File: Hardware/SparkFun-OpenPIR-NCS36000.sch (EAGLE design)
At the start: 33 parts, among them U1 NCS36000, U2 PIR

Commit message: Adding test points to trimpot wipers
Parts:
- added TP1, TP2: TEST-POINT3X5, SparkFun-Connectors:TEST-POINT3X5
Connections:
- net N$7: now also TP1.1
- net VCC: now also TP2.1
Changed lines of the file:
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@@
 <grid distance="0.1" unitdist="inch" unit="inch" style="lines" multiple="1" display="no" altdistance="0.01" altunitdist="inch" altunit="inch"/>
 <layers>
-<layer number="1" name="Top" color="4" fill="1" visible="no" active="no"/>
-<layer number="2" name="Route2" color="1" fill="3" visible="no" active="no"/>
-<layer number="3" name="Route3" color="4" fill="3" visible="no" active="no"/>
-<layer number="4" name="Route4" color="1" fill="4" visible="no" active="no"/>
-<layer number="5" name="Route5" color="4" fill="4" visible="no" active="no"/>
-<layer number="6" name="Route6" color="1" fill="8" visible="no" active="no"/>
-<layer number="7" name="Route7" color="4" fill="8" visible="no" active="no"/>
-<layer number="8" name="Route8" color="1" fill="2" visible="no" active="no"/>
-<layer number="9" name="Route9" color="4" fill="2" visible="no" active="no"/>
-<layer number="10" name="Route10" color="1" fill="7" visible="no" active="no"/>
-<layer number="11" name="Route11" color="4" fill="7" visible="no" active="no"/>
-<layer number="12" name="Route12" color="1" fill="5" visible="no" active="no"/>
-<layer number="13" name="Route13" color="4" fill="5" visible="no" active="no"/>
-<layer number="14" name="Route14" color="1" fill="6" visible="no" active="no"/>
-<layer number="15" name="Route15" color="4" fill="6" visible="no" active="no"/>
-<layer number="16" name="Bottom" color="1" fill="1" visible="no" active="no"/>
-<layer number="17" name="Pads" color="2" fill="1" visible="no" active="no"/>
-<layer number="18" name="Vias" color="2" fill="1" visible="no" active="no"/>
-<layer number="19" name="Unrouted" color="6" fill="1" visible="no" active="no"/>
-<layer number="20" name="Dimension" color="15" fill="1" visible="no" active="no"/>
-<layer number="21" name="tPlace" color="16" fill="1" visible="no" active="no"/>
-<layer number="22" name="bPlace" color="14" fill="1" visible="no" active="no"/>
-<layer number="23" name="tOrigins" color="15" fill="1" visible="no" active="no"/>
-<layer number="24" name="bOrigins" color="15" fill="1" visible="no" active="no"/>
-<layer number="25" name="tNames" color="7" fill="1" visible="no" active="no"/>
-<layer number="26" name="bNames" color="7" fill="1" visible="no" active="no"/>
-<layer number="27" name="tValues" color="7" fill="1" visible="no" active="no"/>
-<layer number="28" name="bValues" color="7" fill="1" visible="no" active="no"/>
+<layer number="1" name="Top" color="4" fill="1" visible="yes" active="no"/>
+<layer number="2" name="Route2" color="1" fill="3" visible="yes" active="no"/>
+<layer number="3" name="Route3" color="4" fill="3" visible="yes" active="no"/>
+<layer number="4" name="Route4" color="1" fill="4" visible="yes" active="no"/>
+<layer number="5" name="Route5" color="4" fill="4" visible="yes" active="no"/>
+<layer number="6" name="Route6" color="1" fill="8" visible="yes" active="no"/>
+<layer number="7" name="Route7" color="4" fill="8" visible="yes" active="no"/>
+<layer number="8" name="Route8" color="1" fill="2" visible="yes" active="no"/>
+<layer number="9" name="Route9" color="4" fill="2" visible="yes" active="no"/>
+<layer number="10" name="Route10" color="1" fill="7" visible="yes" active="no"/>
+<layer number="11" name="Route11" color="4" fill="7" visible="yes" active="no"/>
+<layer number="12" name="Route12" color="1" fill="5" visible="yes" active="no"/>
+<layer number="13" name="Route13" color="4" fill="5" visible="yes" active="no"/>
+<layer number="14" name="Route14" color="1" fill="6" visible="yes" active="no"/>
+<layer number="15" name="Route15" color="4" fill="6" visible="yes" active="no"/>
+<layer number="16" name="Bottom" color="1" fill="1" visible="yes" active="no"/>
+<layer number="17" name="Pads" color="2" fill="1" visible="yes" active="no"/>
+<layer number="18" name="Vias" color="2" fill="1" visible="yes" active="no"/>
+<layer number="19" name="Unrouted" color="6" fill="1" visible="yes" active="no"/>
+<layer number="20" name="Dimension" color="15" fill="1" visible="yes" active="no"/>
+<layer number="21" name="tPlace" color="16" fill="1" visible="yes" active="no"/>
+<layer number="22" name="bPlace" color="14" fill="1" visible="yes" active="no"/>
+<layer number="23" name="tOrigins" color="15" fill="1" visible="yes" active="no"/>
+<layer number="24" name="bOrigins" color="15" fill="1" visible="yes" active="no"/>
+<layer number="25" name="tNames" color="7" fill="1" visible="yes" active="no"/>
+<layer number="26" name="bNames" color="7" fill="1" visible="yes" active="no"/>
+<layer number="27" name="tValues" color="7" fill="1" visible="yes" active="no"/>
+<layer number="28" name="bValues" color="7" fill="1" visible="yes" active="no"/>
 <layer number="29" name="tStop" color="7" fill="3" visible="no" active="no"/>
 <layer number="30" name="bStop" color="7" fill="6" visible="no" active="no"/>
@@
 <layer number="35" name="tGlue" color="7" fill="4" visible="no" active="no"/>
 <layer number="36" name="bGlue" color="7" fill="5" visible="no" active="no"/>
-<layer number="37" name="tTest" color="7" fill="1" visible="no" active="no"/>
-<layer number="38" name="bTest" color="7" fill="1" visible="no" active="no"/>
+<layer number="37" name="tTest" color="7" fill="1" visible="yes" active="no"/>
+<layer number="38" name="bTest" color="7" fill="1" visible="yes" active="no"/>
 <layer number="39" name="tKeepout" color="4" fill="11" visible="no" active="no"/>
 <layer number="40" name="bKeepout" color="1" fill="11" visible="no" active="no"/>
@@
 <layer number="44" name="Drills" color="7" fill="1" visible="no" active="no"/>
 <layer number="45" name="Holes" color="7" fill="1" visible="no" active="no"/>
-<layer number="46" name="Milling" color="3" fill="1" visible="no" active="no"/>
-<layer number="47" name="Measures" color="7" fill="1" visible="no" active="no"/>
-<layer number="48" name="Document" color="7" fill="1" visible="no" active="no"/>
-<layer number="49" name="Reference" color="7" fill="1" visible="no" active="no"/>
-<layer number="50" name="dxf" color="7" fill="1" visible="no" active="no"/>
-<layer number="51" name="tDocu" color="6" fill="1" visible="no" active="no"/>
-<layer number="52" name="bDocu" color="7" fill="1" visible="no" active="no"/>
-<layer number="53" name="tGND_GNDA" color="7" fill="9" visible="no" active="no"/>
-<layer number="54" name="bGND_GNDA" color="1" fill="9" visible="no" active="no"/>
-<layer number="56" name="wert" color="7" fill="1" visible="no" active="no"/>
-<layer number="57" name="tCAD" color="7" fill="1" visible="no" active="no"/>
-<layer number="59" name="tCarbon" color="7" fill="1" visible="no" active="no"/>
-<layer number="60" name="bCarbon" color="7" fill="1" visible="no" active="no"/>
+<layer number="46" name="Milling" color="3" fill="1" visible="yes" active="no"/>
+<layer number="47" name="Measures" color="7" fill="1" visible="yes" active="no"/>
+<layer number="48" name="Document" color="7" fill="1" visible="yes" active="no"/>
+<layer number="49" name="Reference" color="7" fill="1" visible="yes" active="no"/>
+<layer number="50" name="dxf" color="7" fill="1" visible="yes" active="no"/>
+<layer number="51" name="tDocu" color="6" fill="1" visible="yes" active="no"/>
+<layer number="52" name="bDocu" color="7" fill="1" visible="yes" active="no"/>
+<layer number="53" name="tGND_GNDA" color="7" fill="9" visible="yes" active="no"/>
+<layer number="54" name="bGND_GNDA" color="1" fill="9" visible="yes" active="no"/>
+<layer number="56" name="wert" color="7" fill="1" visible="yes" active="no"/>
+<layer number="57" name="tCAD" color="7" fill="1" visible="yes" active="no"/>
+<layer number="59" name="tCarbon" color="7" fill="1" visible="yes" active="no"/>
+<layer number="60" name="bCarbon" color="7" fill="1" visible="yes" active="no"/>
 <layer number="90" name="Modules" color="5" fill="1" visible="yes" active="yes"/>
 <layer number="91" name="Nets" color="2" fill="1" visible="yes" active="yes"/>
@@
 <part name="FD1" library="SparkFun-Aesthetics" deviceset="FIDUCIAL" device="UFIDUCIAL"/>
 <part name="FD2" library="SparkFun-Aesthetics" deviceset="FIDUCIAL" device="UFIDUCIAL"/>
+<part name="TP1" library="SparkFun-Connectors" deviceset="TEST-POINT" device="3X5" value=""/>
+<part name="TP2" library="SparkFun-Connectors" deviceset="TEST-POINT" device="3X5" value=""/>
 </parts>
 <sheets>
@@
 <instance part="FD1" gate="G$1" x="241.3" y="25.4"/>
 <instance part="FD2" gate="G$1" x="238.76" y="27.94"/>
+<instance part="TP1" gate="G$1" x="71.12" y="127" smashed="yes">
+<attribute name="NAME" x="71.12" y="128.016" size="1.778" layer="95" font="vector"/>
+<attribute name="VALUE" x="68.58" y="124.46" size="1.778" layer="96" font="vector"/>
+</instance>
+<instance part="TP2" gate="G$1" x="111.76" y="137.16" smashed="yes" rot="MR0">
+<attribute name="NAME" x="111.76" y="138.176" size="1.778" layer="95" font="vector" rot="MR0"/>
+<attribute name="VALUE" x="114.3" y="134.62" size="1.778" layer="96" font="vector" rot="MR0"/>
+</instance>
 </instances>
 <busses>
@@
 <wire x1="121.92" y1="142.24" x2="121.92" y2="144.78" width="0.1524" layer="91"/>
 <junction x="121.92" y="144.78"/>
+<pinref part="TP2" gate="G$1" pin="1"/>
+<wire x1="111.76" y1="137.16" x2="114.3" y2="137.16" width="0.1524" layer="91"/>
+<junction x="114.3" y="137.16"/>
 </segment>
 </net>
@@
 <wire x1="63.5" y1="119.38" x2="60.96" y2="119.38" width="0.1524" layer="91"/>
 <junction x="60.96" y="119.38"/>
-</segment>
-</net>
+<pinref part="TP1" gate="G$1" pin="1"/>
+<wire x1="71.12" y1="127" x2="68.58" y2="127" width="0.1524" layer="91"/>
+<junction x="68.58" y="127"/>
+</segment>
+</net>

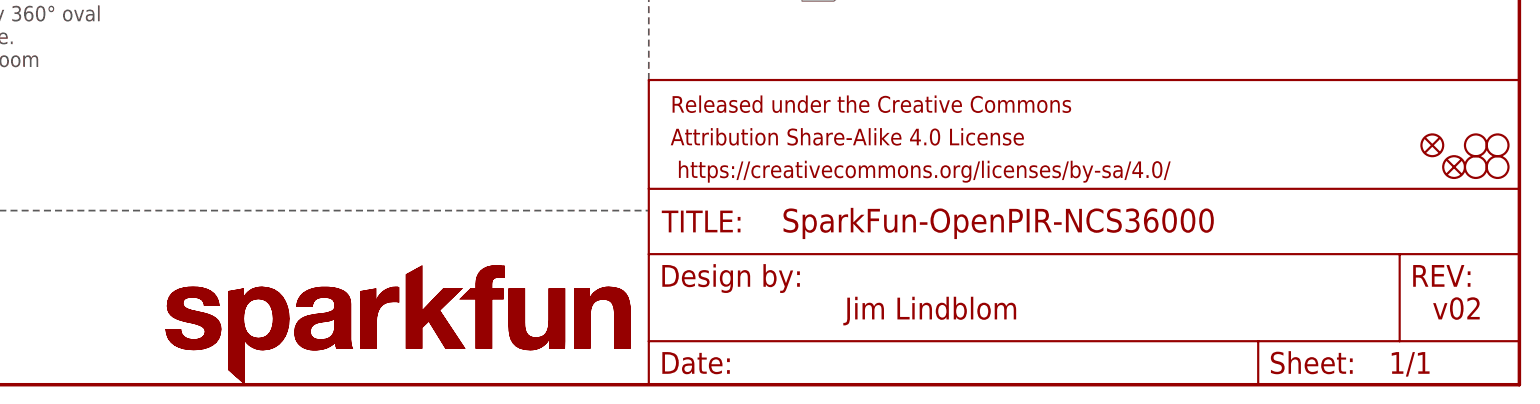
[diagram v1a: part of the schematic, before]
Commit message: Replacing text logo with text+flame, moving schematic fids.
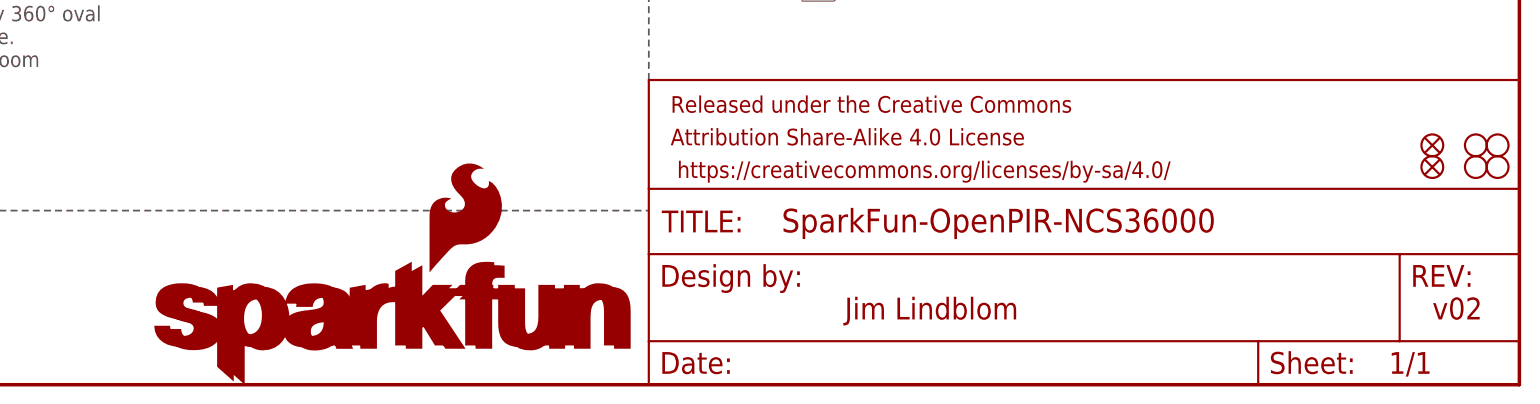
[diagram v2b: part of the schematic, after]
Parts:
- LOGO1: value SFE_LOGO_NAME.1_INCH -> SFE_LOGO_NAME_FLAME.1_INCH; device SparkFun-Aesthetics:SFE_LOGO_NAME.1_INCH -> SparkFun-Aesthetics:SFE_LOGO_NAME_FLAME.1_INCH
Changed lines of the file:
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@@
 <grid distance="0.1" unitdist="inch" unit="inch" style="lines" multiple="1" display="no" altdistance="0.01" altunitdist="inch" altunit="inch"/>
 <layers>
-<layer number="1" name="Top" color="4" fill="1" visible="yes" active="no"/>
-<layer number="2" name="Route2" color="1" fill="3" visible="yes" active="no"/>
-<layer number="3" name="Route3" color="4" fill="3" visible="yes" active="no"/>
-<layer number="4" name="Route4" color="1" fill="4" visible="yes" active="no"/>
-<layer number="5" name="Route5" color="4" fill="4" visible="yes" active="no"/>
-<layer number="6" name="Route6" color="1" fill="8" visible="yes" active="no"/>
-<layer number="7" name="Route7" color="4" fill="8" visible="yes" active="no"/>
-<layer number="8" name="Route8" color="1" fill="2" visible="yes" active="no"/>
-<layer number="9" name="Route9" color="4" fill="2" visible="yes" active="no"/>
-<layer number="10" name="Route10" color="1" fill="7" visible="yes" active="no"/>
-<layer number="11" name="Route11" color="4" fill="7" visible="yes" active="no"/>
-<layer number="12" name="Route12" color="1" fill="5" visible="yes" active="no"/>
-<layer number="13" name="Route13" color="4" fill="5" visible="yes" active="no"/>
-<layer number="14" name="Route14" color="1" fill="6" visible="yes" active="no"/>
-<layer number="15" name="Route15" color="4" fill="6" visible="yes" active="no"/>
-<layer number="16" name="Bottom" color="1" fill="1" visible="yes" active="no"/>
-<layer number="17" name="Pads" color="2" fill="1" visible="yes" active="no"/>
-<layer number="18" name="Vias" color="2" fill="1" visible="yes" active="no"/>
-<layer number="19" name="Unrouted" color="6" fill="1" visible="yes" active="no"/>
-<layer number="20" name="Dimension" color="15" fill="1" visible="yes" active="no"/>
-<layer number="21" name="tPlace" color="16" fill="1" visible="yes" active="no"/>
-<layer number="22" name="bPlace" color="14" fill="1" visible="yes" active="no"/>
-<layer number="23" name="tOrigins" color="15" fill="1" visible="yes" active="no"/>
-<layer number="24" name="bOrigins" color="15" fill="1" visible="yes" active="no"/>
-<layer number="25" name="tNames" color="7" fill="1" visible="yes" active="no"/>
-<layer number="26" name="bNames" color="7" fill="1" visible="yes" active="no"/>
-<layer number="27" name="tValues" color="7" fill="1" visible="yes" active="no"/>
-<layer number="28" name="bValues" color="7" fill="1" visible="yes" active="no"/>
+<layer number="1" name="Top" color="4" fill="1" visible="no" active="no"/>
+<layer number="2" name="Route2" color="1" fill="3" visible="no" active="no"/>
+<layer number="3" name="Route3" color="4" fill="3" visible="no" active="no"/>
+<layer number="4" name="Route4" color="1" fill="4" visible="no" active="no"/>
+<layer number="5" name="Route5" color="4" fill="4" visible="no" active="no"/>
+<layer number="6" name="Route6" color="1" fill="8" visible="no" active="no"/>
+<layer number="7" name="Route7" color="4" fill="8" visible="no" active="no"/>
+<layer number="8" name="Route8" color="1" fill="2" visible="no" active="no"/>
+<layer number="9" name="Route9" color="4" fill="2" visible="no" active="no"/>
+<layer number="10" name="Route10" color="1" fill="7" visible="no" active="no"/>
+<layer number="11" name="Route11" color="4" fill="7" visible="no" active="no"/>
+<layer number="12" name="Route12" color="1" fill="5" visible="no" active="no"/>
+<layer number="13" name="Route13" color="4" fill="5" visible="no" active="no"/>
+<layer number="14" name="Route14" color="1" fill="6" visible="no" active="no"/>
+<layer number="15" name="Route15" color="4" fill="6" visible="no" active="no"/>
+<layer number="16" name="Bottom" color="1" fill="1" visible="no" active="no"/>
+<layer number="17" name="Pads" color="2" fill="1" visible="no" active="no"/>
+<layer number="18" name="Vias" color="2" fill="1" visible="no" active="no"/>
+<layer number="19" name="Unrouted" color="6" fill="1" visible="no" active="no"/>
+<layer number="20" name="Dimension" color="15" fill="1" visible="no" active="no"/>
+<layer number="21" name="tPlace" color="16" fill="1" visible="no" active="no"/>
+<layer number="22" name="bPlace" color="14" fill="1" visible="no" active="no"/>
+<layer number="23" name="tOrigins" color="15" fill="1" visible="no" active="no"/>
+<layer number="24" name="bOrigins" color="15" fill="1" visible="no" active="no"/>
+<layer number="25" name="tNames" color="7" fill="1" visible="no" active="no"/>
+<layer number="26" name="bNames" color="7" fill="1" visible="no" active="no"/>
+<layer number="27" name="tValues" color="7" fill="1" visible="no" active="no"/>
+<layer number="28" name="bValues" color="7" fill="1" visible="no" active="no"/>
 <layer number="29" name="tStop" color="7" fill="3" visible="no" active="no"/>
 <layer number="30" name="bStop" color="7" fill="6" visible="no" active="no"/>
@@
 <layer number="35" name="tGlue" color="7" fill="4" visible="no" active="no"/>
 <layer number="36" name="bGlue" color="7" fill="5" visible="no" active="no"/>
-<layer number="37" name="tTest" color="7" fill="1" visible="yes" active="no"/>
-<layer number="38" name="bTest" color="7" fill="1" visible="yes" active="no"/>
+<layer number="37" name="tTest" color="7" fill="1" visible="no" active="no"/>
+<layer number="38" name="bTest" color="7" fill="1" visible="no" active="no"/>
 <layer number="39" name="tKeepout" color="4" fill="11" visible="no" active="no"/>
 <layer number="40" name="bKeepout" color="1" fill="11" visible="no" active="no"/>
@@
 <layer number="44" name="Drills" color="7" fill="1" visible="no" active="no"/>
 <layer number="45" name="Holes" color="7" fill="1" visible="no" active="no"/>
-<layer number="46" name="Milling" color="3" fill="1" visible="yes" active="no"/>
-<layer number="47" name="Measures" color="7" fill="1" visible="yes" active="no"/>
-<layer number="48" name="Document" color="7" fill="1" visible="yes" active="no"/>
-<layer number="49" name="Reference" color="7" fill="1" visible="yes" active="no"/>
-<layer number="50" name="dxf" color="7" fill="1" visible="yes" active="no"/>
-<layer number="51" name="tDocu" color="6" fill="1" visible="yes" active="no"/>
-<layer number="52" name="bDocu" color="7" fill="1" visible="yes" active="no"/>
-<layer number="53" name="tGND_GNDA" color="7" fill="9" visible="yes" active="no"/>
-<layer number="54" name="bGND_GNDA" color="1" fill="9" visible="yes" active="no"/>
-<layer number="56" name="wert" color="7" fill="1" visible="yes" active="no"/>
-<layer number="57" name="tCAD" color="7" fill="1" visible="yes" active="no"/>
-<layer number="59" name="tCarbon" color="7" fill="1" visible="yes" active="no"/>
-<layer number="60" name="bCarbon" color="7" fill="1" visible="yes" active="no"/>
+<layer number="46" name="Milling" color="3" fill="1" visible="no" active="no"/>
+<layer number="47" name="Measures" color="7" fill="1" visible="no" active="no"/>
+<layer number="48" name="Document" color="7" fill="1" visible="no" active="no"/>
+<layer number="49" name="Reference" color="7" fill="1" visible="no" active="no"/>
+<layer number="50" name="dxf" color="7" fill="1" visible="no" active="no"/>
+<layer number="51" name="tDocu" color="6" fill="1" visible="no" active="no"/>
+<layer number="52" name="bDocu" color="7" fill="1" visible="no" active="no"/>
+<layer number="53" name="tGND_GNDA" color="7" fill="9" visible="no" active="no"/>
+<layer number="54" name="bGND_GNDA" color="1" fill="9" visible="no" active="no"/>
+<layer number="56" name="wert" color="7" fill="1" visible="no" active="no"/>
+<layer number="57" name="tCAD" color="7" fill="1" visible="no" active="no"/>
+<layer number="59" name="tCarbon" color="7" fill="1" visible="no" active="no"/>
+<layer number="60" name="bCarbon" color="7" fill="1" visible="no" active="no"/>
 <layer number="90" name="Modules" color="5" fill="1" visible="yes" active="yes"/>
 <layer number="91" name="Nets" color="2" fill="1" visible="yes" active="yes"/>
@@
 <part name="R7" library="openPIR-temp" deviceset="TRIMPOT" device="TX33X-1M" value="1M"/>
 <part name="R6" library="openPIR-temp" deviceset="51KOHM" device="-0603-1/10W-1%" value="51k"/>
-<part name="LOGO1" library="SparkFun-Aesthetics" deviceset="SFE_LOGO_NAME" device=".1_INCH"/>
+<part name="LOGO1" library="SparkFun-Aesthetics" deviceset="SFE_LOGO_NAME_FLAME" device=".1_INCH"/>
 <part name="LOGO3" library="SparkFun-Aesthetics" deviceset="SFE_LOGO_NAME" device=".1_INCH"/>
 <part name="LOGO4" library="SparkFun-Aesthetics" deviceset="OSHW-LOGO" device="S" value="OSHW-LOGOS"/>
@@
 <instance part="J8" gate="G$1" x="203.2" y="139.7" rot="MR0"/>
 <instance part="J2" gate="G$1" x="203.2" y="165.1" rot="MR0"/>
-<instance part="FD1" gate="G$1" x="241.3" y="25.4"/>
-<instance part="FD2" gate="G$1" x="238.76" y="27.94"/>
+<instance part="FD1" gate="G$1" x="238.76" y="27.94"/>
+<instance part="FD2" gate="G$1" x="238.76" y="25.4"/>
 <instance part="TP1" gate="G$1" x="71.12" y="127" smashed="yes">
 <attribute name="NAME" x="71.12" y="128.016" size="1.778" layer="95" font="vector"/>
